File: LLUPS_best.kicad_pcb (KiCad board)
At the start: 2 copper layers, 140 x 90 mm, 39 parts, among them J1 USB_C, J2 Output, J3 Debug, Q1 FS8205A, U1 USBLC6-2SC6, U2 BQ24072, U3 HY2113-KB5B, U4 MT3608, U5 AP2112K-3.3, U6 LN61CN3302MR-G

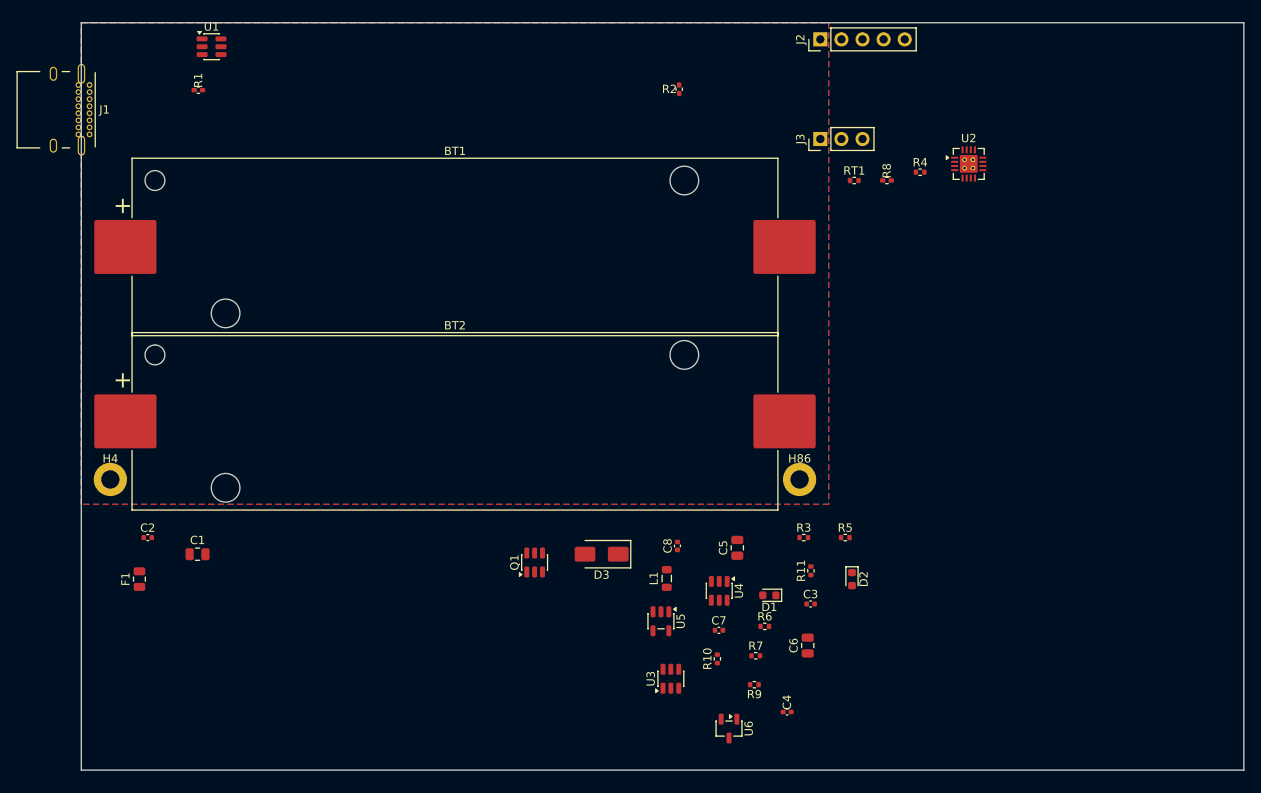
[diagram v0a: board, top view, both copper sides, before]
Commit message: Fix battery holder footprint to match BOM
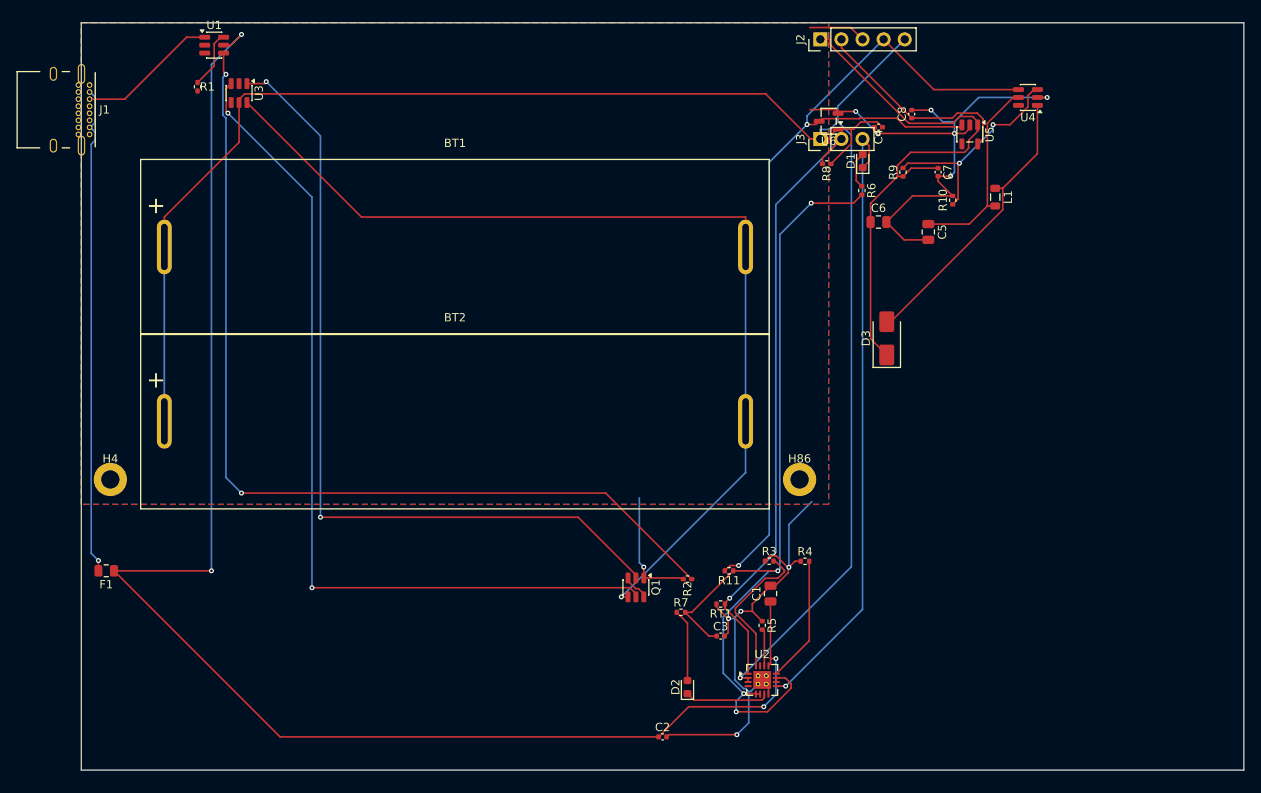
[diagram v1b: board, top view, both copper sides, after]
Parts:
- BT1, BT2: footprint Battery:BatteryHolder_Keystone_1042_1x18650 -> LLUPS:BatteryHolder_MYOUNG_BH-18650-A1AJ006
- moved U3 87.6 mm to (19.0, 8.47), turned to -90 degrees
- moved U6 74.1 mm to (90.0, 11.9), turned to 180 degrees
- moved C4 71.3 mm to (96.0, 12.6), turned to 180 degrees
- moved U4 70.1 mm to (114.0, 9.00), turned to 180 degrees
- moved U5 69.4 mm to (107.0, 13.4)
- moved C1 69.2 mm to (83.0, 68.7), turned to 90 degrees
- moved U2 66.9 mm to (82.0, 79.1)
- moved C2 66.5 mm to (70.0, 86.0)
- moved R9 64.3 mm to (99.0, 18.0), turned to 90 degrees
- moved R10 62.1 mm to (104.9, 21.4)
- moved C7 61.2 mm to (103.2, 18.0), turned to -90 degrees
- moved L1 60.6 mm to (110.1, 21.0), turned to -90 degrees
- moved C8 59.2 mm to (100.0, 11.0)
- moved R2 59.0 mm to (73.0, 67.0), turned to 180 degrees
- moved R6 53.8 mm to (94.0, 20.2), turned to -90 degrees
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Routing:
- net /VBAT: track 0.00 -> 220.5 mm, vias 0 -> 1
- net /VBUS: track 0.00 -> 183.5 mm, vias 0 -> 4
- net GND: track 0.00 -> 151.8 mm, vias 0 -> 11
- net /CELL_NEG: track 0.00 -> 118.5 mm, vias 0 -> 1
- net Net-(R2-Pad1): track 0.00 -> 112.7 mm, vias 0 -> 2
- net /EN: track 0.00 -> 110.8 mm, vias 0 -> 2
- net /VSYS: track 0.00 -> 105.3 mm, vias 0 -> 4
- net Net-(Q1B-G): track 0.00 -> 104.9 mm, vias 0 -> 2
- net Net-(Q1A-G): track 0.00 -> 98.8 mm, vias 0 -> 2
- net /NTC_SENSE: track 0.00 -> 75.3 mm, vias 0 -> 1
- net /CHG_N: track 0.00 -> 75.0 mm, vias 0 -> 1
- net /5V: track 0.00 -> 67.4 mm
- net Net-(F1-Pad2): track 0.00 -> 59.1 mm, vias 0 -> 1
- net Net-(D3-A): track 0.00 -> 34.8 mm
- net Net-(U4-FB): track 0.00 -> 26.5 mm, vias 0 -> 2
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
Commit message: Remove old Python autorouter, clean references, update docs
Deleted:
- simple_router.py, reroute_net.py, _apply_routing.py (old A*/RRR router)
- BUGFIX_PLAN.md, IMPROVEMENT_PLAN.md (old planning docs)
- freerouting-plan.md, dashboard-automation.md (completed migration docs)
- experiments_dashboard.png (stale artifact)

Cleaned:
- autoroute.py: removed dead --no-rrr flag
- diff_rounds.py: removed A* Expansions and RRR timing fields
- generate_report.py: removed RRR timing and a_star_expansions column
- plot_experiments.py: removed RRR bar from timing chart
- SKILL.md: removed old router references from observability section

Updated docs:
- next-steps.md: rewritten for current state (150-round run complete)
- monitoring-guide.md: fixed timing chart description
- CHANGELOG.md: documented cleanup

Also includes: FreeRouting migration code changes (types.py, pipeline.py,
freerouting_runner.py, adapter.py), 150-round experiment results, and
updated architecture/auto-trace/README docs from prior sessions.
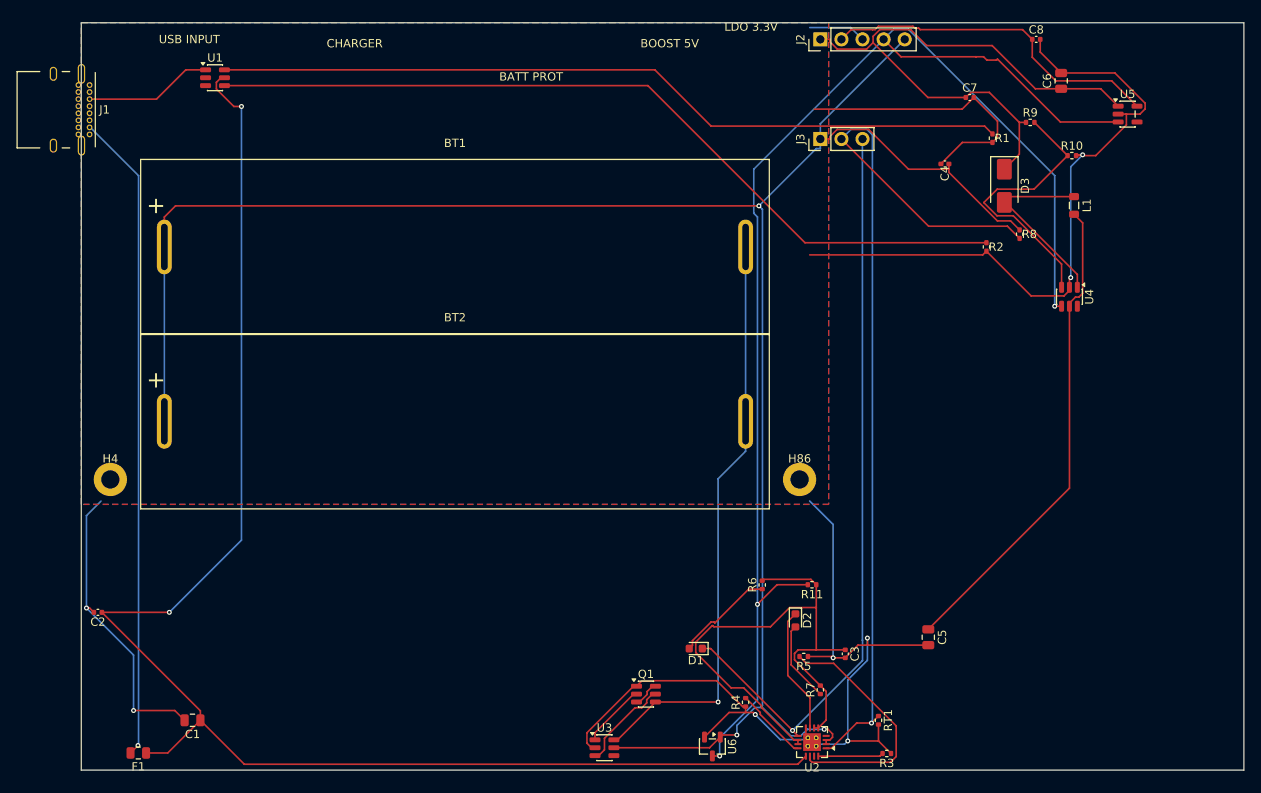
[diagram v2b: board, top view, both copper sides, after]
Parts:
- moved R1 95.9 mm to (109.7, 13.9)
- moved U3 90.3 mm to (63.0, 87.3), turned to 0 degrees
- moved U6 76.6 mm to (76.0, 87.2), turned to -90 degrees
- moved C1 71.3 mm to (13.4, 84.0), turned to 180 degrees
- moved C2 69.6 mm to (2.00, 71.0), turned to 180 degrees
- moved D1 62.1 mm to (74.0, 75.4), turned to 180 degrees
- moved R2 53.8 mm to (109.0, 27.0), turned to -90 degrees
- moved R6 49.0 mm to (82.0, 67.7), turned to 90 degrees
- moved C5 48.8 mm to (102.0, 74.0)
- moved C6 27.8 mm to (118.0, 7.00), turned to 90 degrees
- moved R3 27.1 mm to (97.0, 88.0), turned to 180 degrees
- moved R8 24.7 mm to (113.0, 25.5), turned to -90 degrees
- moved U4 24.5 mm to (119.0, 33.0), turned to -90 degrees
- moved RT1 23.6 mm to (96.0, 84.0), turned to -90 degrees
- moved D3 23.2 mm to (111.2, 19.6), turned to -90 degrees
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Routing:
- net GND: track 151.8 -> 266.0 mm, vias 11 -> 8
- net Net-(Q1B-G): track 104.9 -> 11.4 mm, vias 2 -> 0
- net Net-(Q1A-G): track 98.8 -> 7.78 mm, vias 2 -> 0
- net Net-(R1-Pad1): track 6.96 -> 95.7 mm
- net /EN: track 110.8 -> 180.2 mm, vias 2 -> 3
- net /CELL_NEG: track 118.5 -> 70.6 mm
- net /VSYS: track 105.3 -> 67.3 mm, vias 4 -> 0
- net /NTC_SENSE: track 75.3 -> 109.7 mm
- net /VSYS_BOOST: track 24.0 -> 58.4 mm
- net /VBAT: track 220.5 -> 248.3 mm, vias 1 -> 3
- net Net-(U2-TMR): track 4.46 -> 30.1 mm
- net Net-(F1-Pad2): track 59.1 -> 78.2 mm
- net /3V3: track 25.4 -> 41.5 mm
- net /CHG_N: track 75.0 -> 90.6 mm
- net Net-(R2-Pad1): track 112.7 -> 99.6 mm, vias 2 -> 0
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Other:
- board text added: "BATT PROT"
- board text added: "BOOST 5V"
- board text added: "CHARGER"
- board text added: "LDO 3.3V"
- board text added: "USB INPUT"
